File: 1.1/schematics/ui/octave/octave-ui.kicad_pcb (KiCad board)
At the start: 2 copper layers, 100 x 30 mm, 7 parts

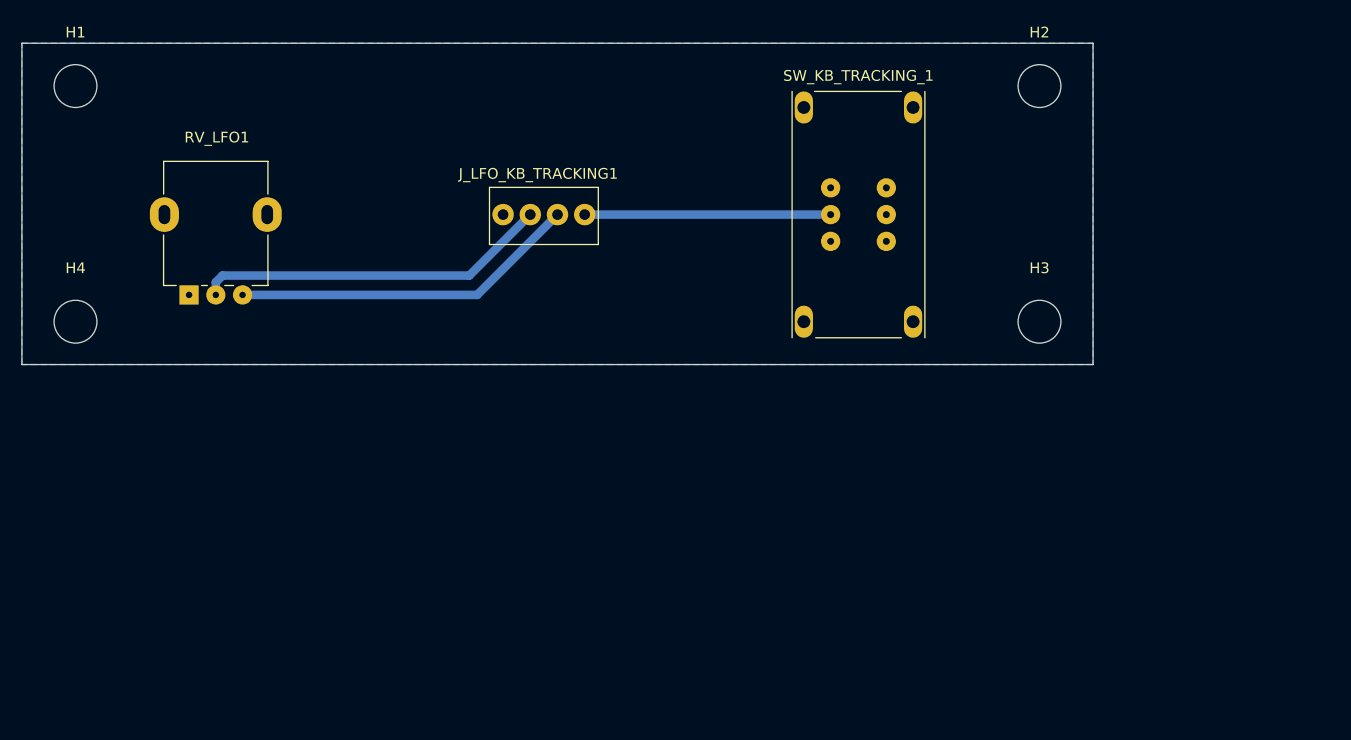
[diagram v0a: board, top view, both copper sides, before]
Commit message: Added chord logic (untested)
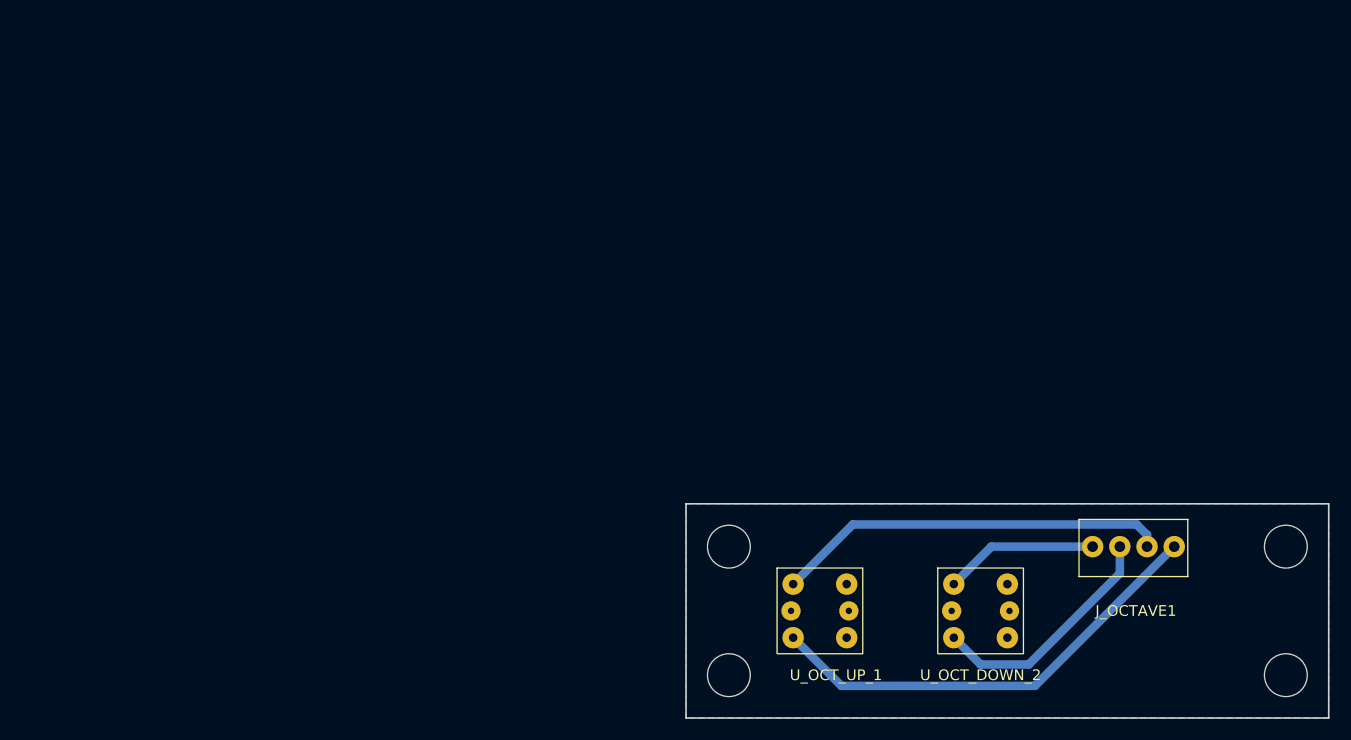
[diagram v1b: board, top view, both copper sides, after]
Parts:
- removed J_LFO_KB_TRACKING1: Conn_01x04, Shmoergh_Custom_Footprints:NSL25_01x04_Vertical
- removed RV_LFO1: 100k, Shmoergh_Custom_Footprints:Potentiometer_Alpha_RD901F-40-00D_Single_Vertical
- removed SW_KB_TRACKING_1: SW_DPDT_x2, Shmoergh_Custom_Footprints:DPDT Korg Style Switch
- added J_OCTAVE1: Conn_01x04, Shmoergh_Custom_Footprints:NSL25_01x04_Vertical, F.Cu at (174.6, 93.0)
- added U_OCT_DOWN_2: SW_SPST_Push_LED, Shmoergh_Custom_Footprints:SPST_Narrow_Circular_Pushbutton_LED, F.Cu at (156.5, 99.0)
- added U_OCT_UP_1: SW_SPST_Push_LED, Shmoergh_Custom_Footprints:SPST_Narrow_Circular_Pushbutton_LED, F.Cu at (141.5, 99.0)
- moved H1 125.7 mm to (185.0, 105.0)
- moved H4 64.5 mm to (133.0, 93.0)
- moved H2 48.8 mm to (185.0, 93.0)
- moved H3 43.9 mm to (133.0, 105.0)
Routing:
- net OCT_UP_1: track 0.00 -> 42.8 mm
- net OCT_UP_2: track 0.00 -> 36.8 mm
- net LFO_OUT: track 33.2 -> 0.00 mm
- net LFO_IN: track 32.6 -> 0.00 mm
- net KB_TRACKING: track 23.0 -> 0.00 mm
- net OCT_DOWN_1: track 0.00 -> 22.6 mm
- net OCT_DOWN_2: track 0.00 -> 14.4 mm
- added copper zone on B.Cu, net (none)
- removed copper zone on B.Cu, net GND
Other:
- board size 100 x 30 mm -> 60 x 20 mm
